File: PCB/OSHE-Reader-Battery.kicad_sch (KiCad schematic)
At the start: 20 parts, among them J1 Conn_01x03, Q3 PMOS, Q4 PNP, U2 BQ2057CSNTR

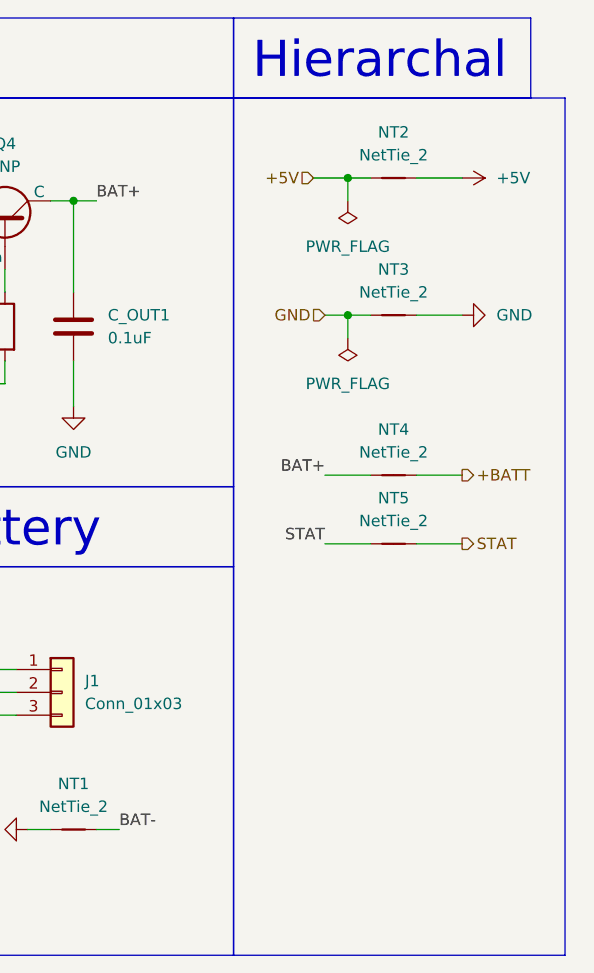
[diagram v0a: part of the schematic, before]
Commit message: added VBUS port on battery-charger section
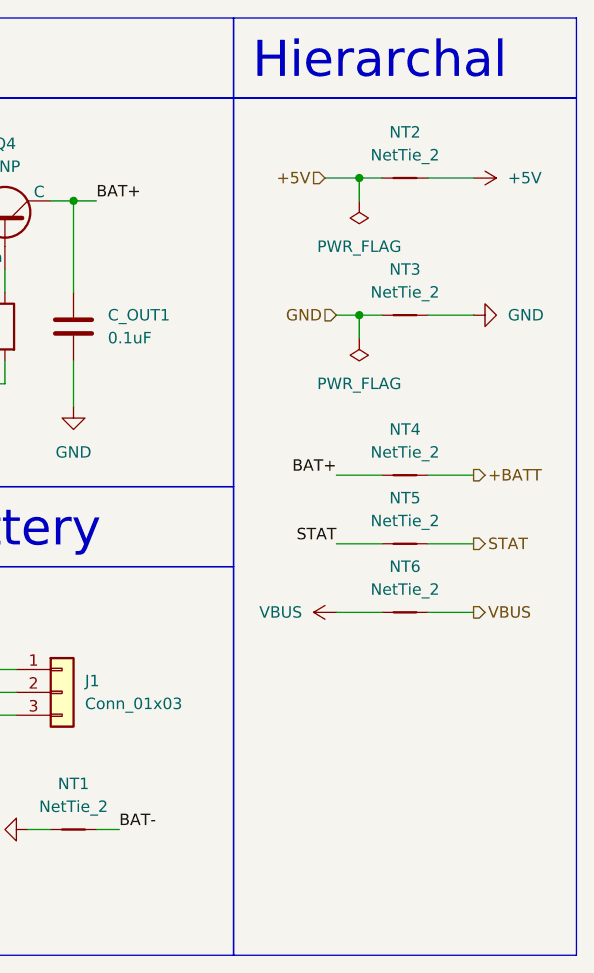
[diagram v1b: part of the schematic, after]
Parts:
- added NT6: NetTie_2, symbol Device:NetTie_2
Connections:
- net VBUS: now also NT6.1, NT6.2
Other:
- moved on the sheet: NT2, NT3, NT4, NT5

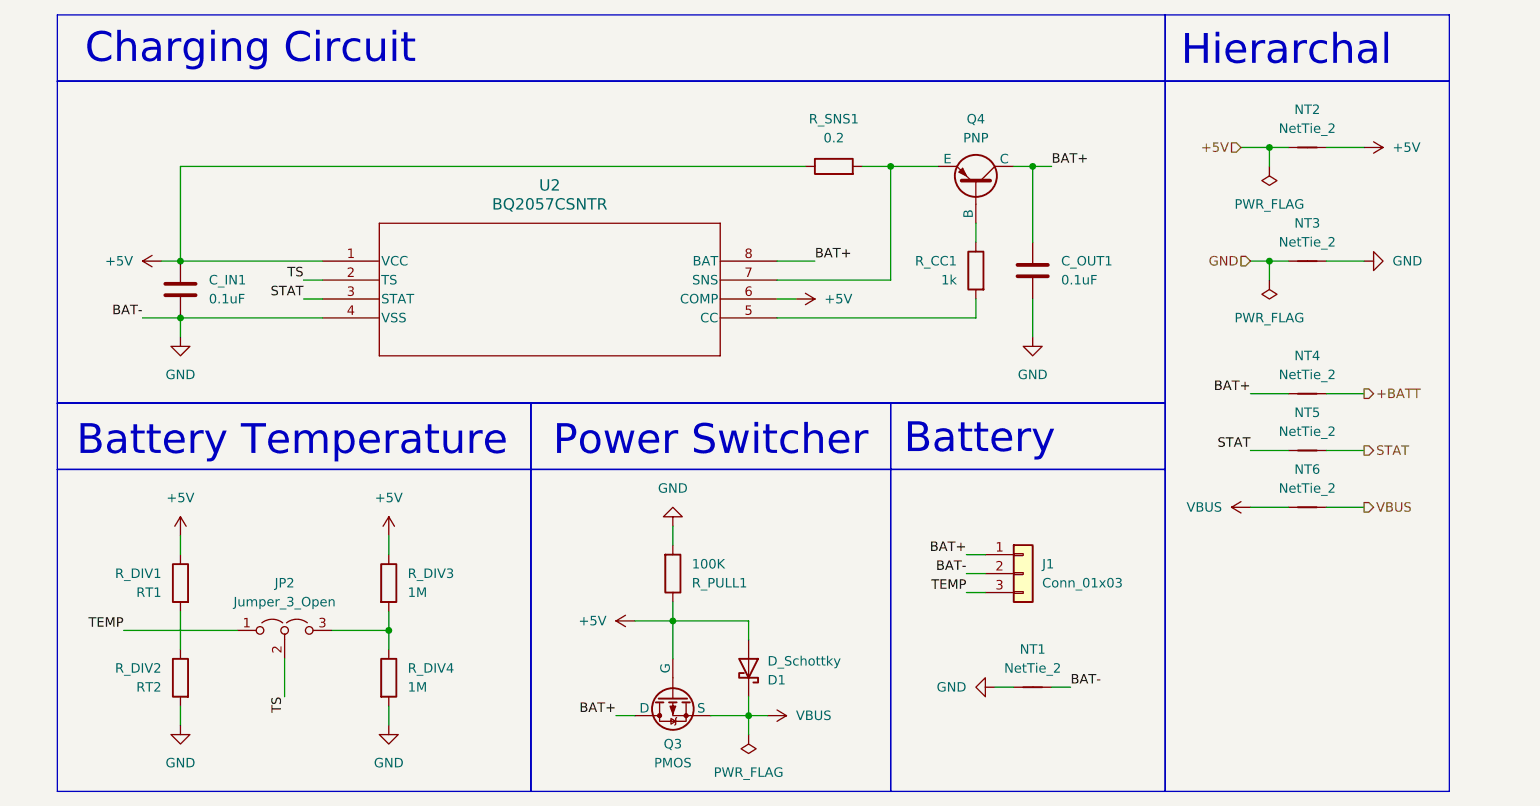
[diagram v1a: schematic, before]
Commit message: refactored battery charger, added usb-c port sheet
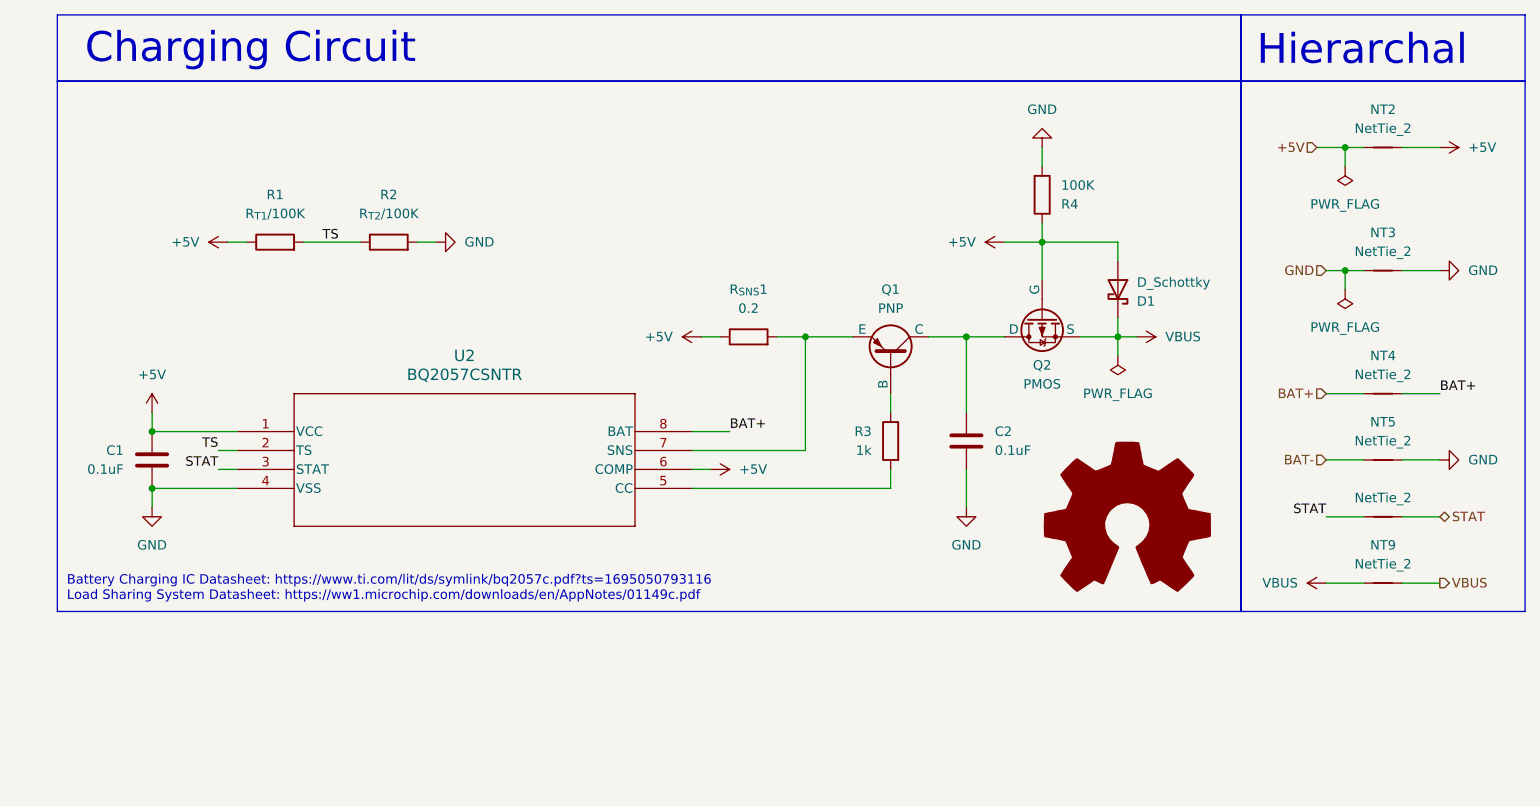
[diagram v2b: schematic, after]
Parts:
- removed C_IN1: 0.1uF, symbol Device:C
- removed J1: Conn_01x03, symbol Connector_Generic:Conn_01x03
- removed JP2: Jumper_3_Open, symbol Jumper:Jumper_3_Open
- removed NT1: NetTie_2, symbol Device:NetTie_2
- removed R_DIV1: RT1, symbol Device:R
- removed R_DIV2: RT2, symbol Device:R
- removed R_DIV3, R_DIV4: 1M, symbol Device:R
- added C1: 0.1uF, symbol Device:C
- added NT7: NetTie_2, symbol Device:NetTie_2
- added R1: R_{T1}/100K, symbol Device:R
- added R2: R_{T2}/100K, symbol Device:R
- renumbered C_OUT1 to C2, NT6 to NT9, Q4 to Q1, Q3 to Q2, R_CC1 to R3, R_PULL1 to R4, R_SNS1 to R_{SNS}1
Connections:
- net +BATT is gone; now on net BAT+: NT4.2
- net +5V: now also C1.1, R1.1
- net BAT+: no longer C2.1, Q1.1 (C), Q2.1 (D)
- net GND: now also NT5.2, C1.2, R2.2
- net STAT: now also NT7.1, NT7.2; no longer NT5.1, NT5.2
- net TS: now also R1.2, R2.1
- new net: C2.1, Q1.1 (C), Q2.1 (D)
- new net BAT-: NT5.1
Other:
- note added: "Battery Charging IC Datasheet: https://www.ti.com/lit/ds/symlink/bq2057c.pdf?ts=1695050793116 Load Sharing System Datasheet: https://ww1.microchip.com/downloads/en/AppNotes/01149c.pdf"
- note removed: "Battery"
- note removed: "Battery Temperature"
- note removed: "Power Switcher"
- moved on the sheet: C2, D1, NT2, NT3, NT9, Q1, Q2, R3, R4, R_{SNS}1, U2
